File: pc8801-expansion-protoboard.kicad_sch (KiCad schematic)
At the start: 42 parts, among them J1 Solder Side, J2 Parts Side, J3 5V, J4 12V, J5 -12V, J6 GND_1, J7 GND_2, SW1 Reset ESP, U1 ExpansionEdge, U10 74LS165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

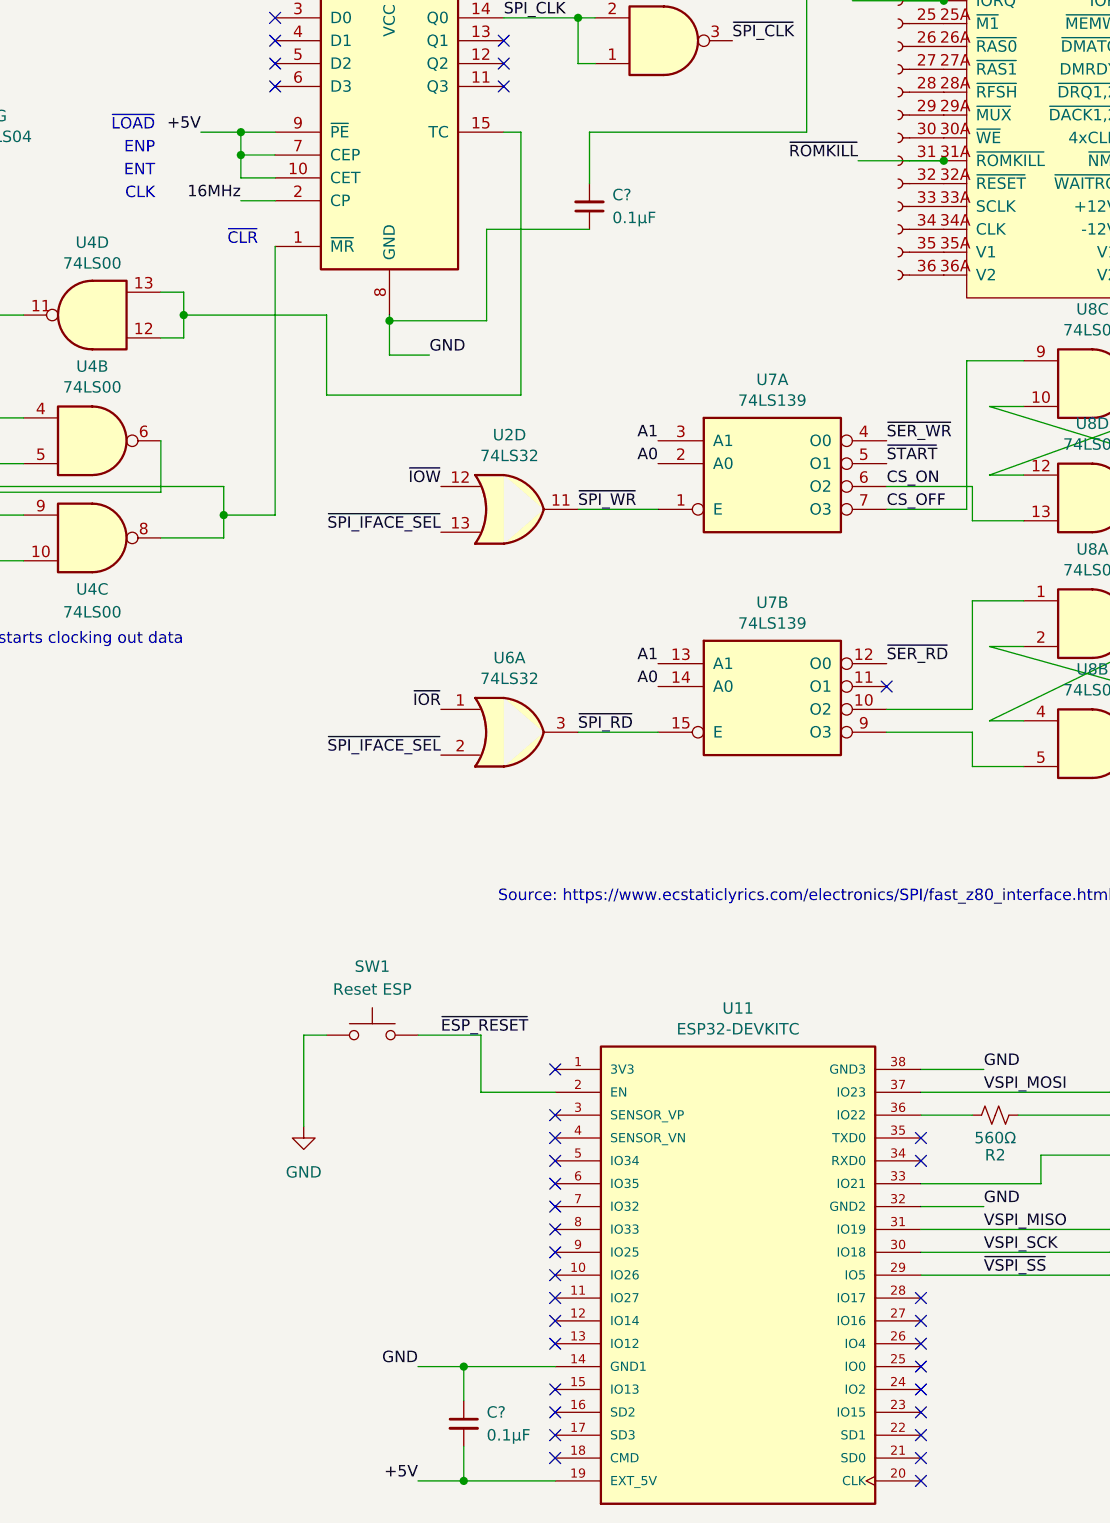
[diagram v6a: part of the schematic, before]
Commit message: Wire ESP32 to system reset
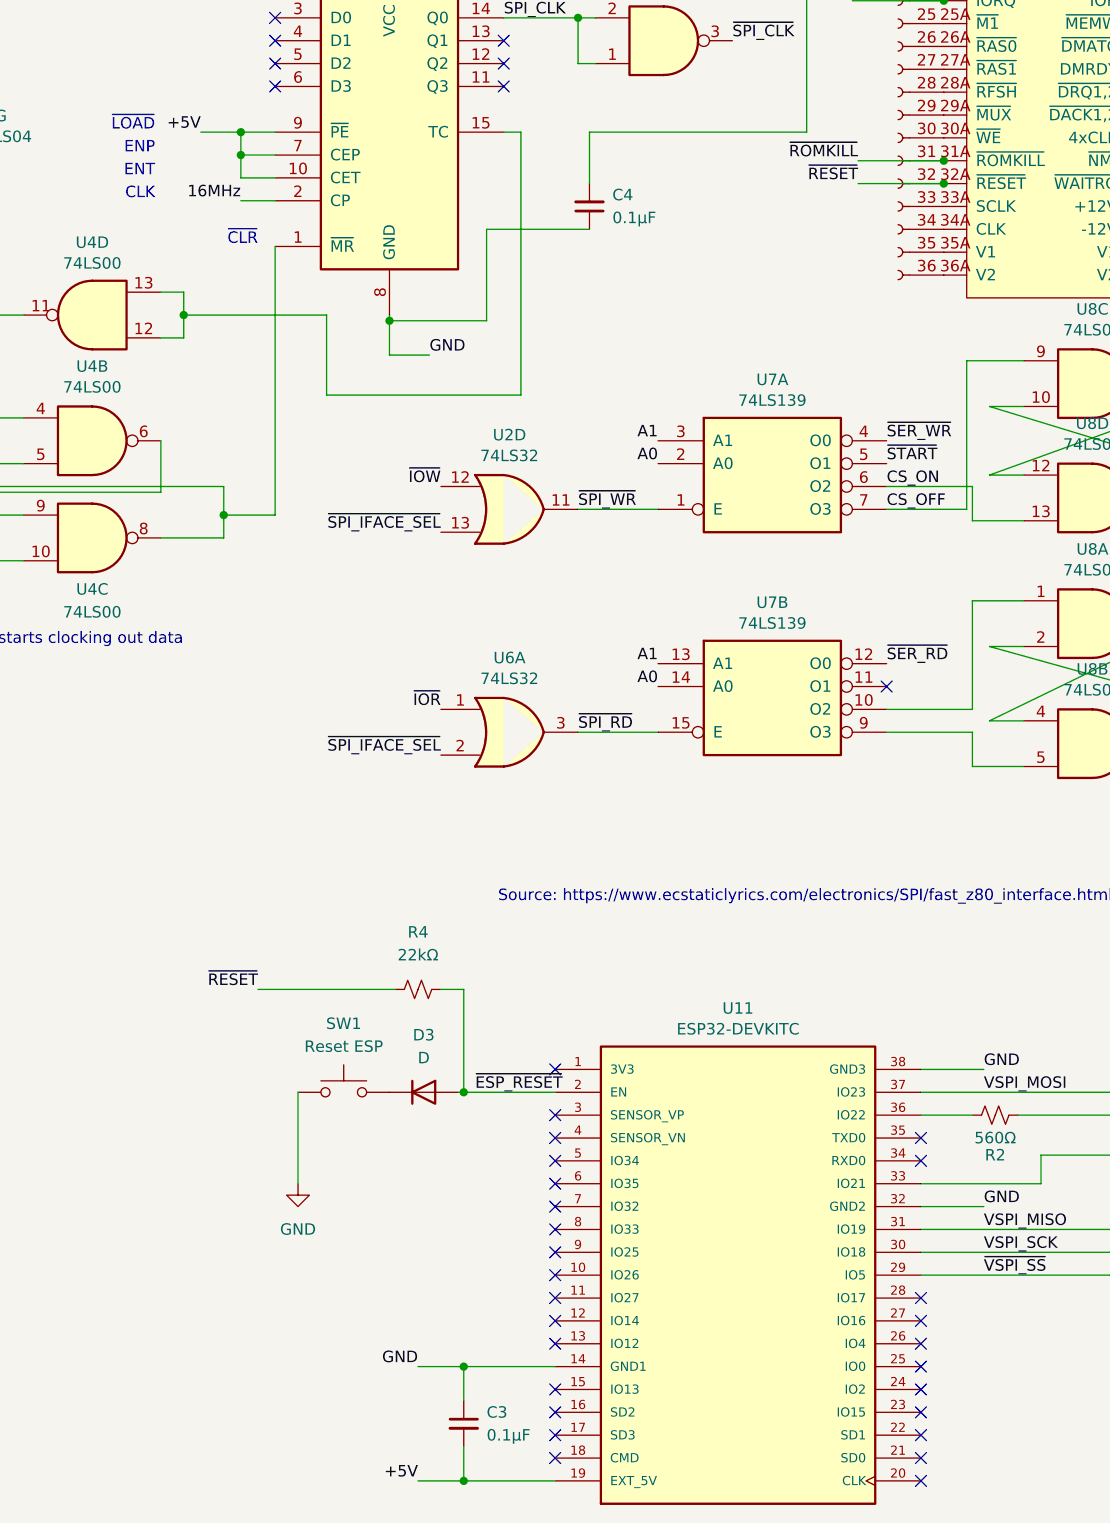
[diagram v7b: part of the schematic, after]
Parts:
- added D3: D, Diode_THT:D_A-405_P10.16mm_Horizontal, symbol Device:D
- added R4: 22kΩ, Resistor_THT:R_Axial_DIN0207_L6.3mm_D2.5mm_P10.16mm_Horizontal, symbol Device:R_Small_US
- gave numbers to parts that had none: 2
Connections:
- net ~{ESP_RESET}: now also D3.2 (A), R4.2; no longer SW1.2
- net ~{RESET}: now reaches J1.32 (Pin_32), U1.32A (~{RESET})
- net ~{RESET}: now also R4.1
- new net: D3.1 (K), SW1.2
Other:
- moved on the sheet: SW1
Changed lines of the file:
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@@
   (junction (at 135.89 60.325) (diameter 0) (color 0 0 0 0)
   )
+  (junction (at 82.55 227.33) (diameter 0) (color 0 0 0 0)
+  )
   (junction (at 135.89 123.825) (diameter 0) (color 0 0 0 0)
   )
@@
   )
   (junction (at 158.75 80.645) (diameter 0) (color 0 0 0 0)
+  )
+  (junction (at 135.89 126.365) (diameter 0) (color 0 0 0 0)
   )
   (junction (at 178.435 47.625) (diameter 0) (color 0 0 0 0)
@@
     (stroke (width 0) (type default) (color 0 0 0 0))
   )
-  (wire (pts (xy 84.455 227.33) (xy 84.455 220.98))
-    (stroke (width 0) (type default) (color 0 0 0 0))
-  )
   (wire (pts (xy 135.89 70.485) (xy 111.76 70.485))
     (stroke (width 0) (type default) (color 0 0 0 0))
@@
     (stroke (width 0) (type default) (color 0 0 0 0))
   )
+  (wire (pts (xy 80.01 215.9) (xy 82.55 215.9))
+    (stroke (width 0) (type default) (color 0 0 0 0))
+  )
   (wire (pts (xy 138.43 146.05) (xy 144.78 146.05))
     (stroke (width 0) (type default) (color 0 0 0 0))
@@
     (stroke (width 0) (type default) (color 0 0 0 0))
   )
+  (wire (pts (xy 82.55 215.9) (xy 82.55 227.33))
+    (stroke (width 0) (type default) (color 0 0 0 0))
+  )
   (wire (pts (xy 231.14 133.35) (xy 253.365 133.35))
     (stroke (width 0) (type default) (color 0 0 0 0))
@@
     (stroke (width 0) (type default) (color 0 0 0 0))
   )
-  (wire (pts (xy 64.77 220.98) (xy 67.31 220.98))
+  (wire (pts (xy 59.69 215.9) (xy 74.93 215.9))
     (stroke (width 0) (type default) (color 0 0 0 0))
   )
@@
     (stroke (width 0) (type default) (color 0 0 0 0))
   )
+  (wire (pts (xy 82.55 227.33) (xy 92.71 227.33))
+    (stroke (width 0) (type default) (color 0 0 0 0))
+  )
   (wire (pts (xy 303.53 114.3) (xy 305.435 114.3))
     (stroke (width 0) (type default) (color 0 0 0 0))
@@
     (stroke (width 0) (type default) (color 0 0 0 0))
   )
-  (wire (pts (xy 64.77 231.14) (xy 64.77 220.98))
+  (wire (pts (xy 64.135 237.49) (xy 64.135 227.33))
     (stroke (width 0) (type default) (color 0 0 0 0))
   )
@@
     (stroke (width 0) (type default) (color 0 0 0 0))
   )
-  (wire (pts (xy 92.71 227.33) (xy 84.455 227.33))
+  (wire (pts (xy 81.915 227.33) (xy 82.55 227.33))
     (stroke (width 0) (type default) (color 0 0 0 0))
   )
@@
     (stroke (width 0) (type default) (color 0 0 0 0))
   )
+  (wire (pts (xy 126.365 126.365) (xy 135.89 126.365))
+    (stroke (width 0) (type default) (color 0 0 0 0))
+  )
   (wire (pts (xy 209.55 133.35) (xy 187.325 133.35))
     (stroke (width 0) (type default) (color 0 0 0 0))
@@
   )
   (wire (pts (xy 158.75 85.725) (xy 188.595 85.725))
-    (stroke (width 0) (type default) (color 0 0 0 0))
-  )
-  (wire (pts (xy 84.455 220.98) (xy 77.47 220.98))
     (stroke (width 0) (type default) (color 0 0 0 0))
   )
@@
     (effects (font (size 1.27 1.27)) (justify right bottom))
   )
+  (label "~{RESET}" (at 126.365 126.365 180)
+    (effects (font (size 1.27 1.27)) (justify right bottom))
+  )
   (label "~{IORQ}" (at 125.73 106.045 180)
     (effects (font (size 1.27 1.27)) (justify right bottom))
@@
     (effects (font (size 1.27 1.27)) (justify left bottom))
   )
+  (label "~{RESET}" (at 59.69 215.9 180)
+    (effects (font (size 1.27 1.27)) (justify right bottom))
+  )
   (label "SPI_CLK" (at 86.995 107.95 0)
     (effects (font (size 1.27 1.27)) (justify left bottom))
@@
     (effects (font (size 1.27 1.27)) (justify left bottom))
   )
-  (label "~{ESP_RESET}" (at 80.01 220.98 0)
+  (label "~{ESP_RESET}" (at 83.82 227.33 0)
     (effects (font (size 1.27 1.27)) (justify left bottom))
   )
@@
   (symbol (lib_id "Device:C_Small") (at 82.55 264.16 0) (mirror y) (unit 1)
     (in_bom yes) (on_board yes) (fields_autoplaced)
-    (property "Reference" "C?" (id 0) (at 85.09 262.8962 0)
+    (property "Reference" "C3" (id 0) (at 85.09 262.8962 0)
       (effects (font (size 1.27 1.27)) (justify right))
     )
@@
     (pin "2")
   )
-  (symbol (lib_id "power:GND") (at 64.77 231.14 0) (unit 1)
+  (symbol (lib_id "power:GND") (at 64.135 237.49 0) (unit 1)
     (in_bom yes) (on_board yes) (fields_autoplaced)
-    (property "Reference" "#PWR0101" (id 0) (at 64.77 237.49 0)
-      (effects (font (size 1.27 1.27)) hide)
-    )
-    (property "Value" "GND" (id 1) (at 64.77 236.22 0))
-    (property "Footprint" "" (id 2) (at 64.77 231.14 0)
-      (effects (font (size 1.27 1.27)) hide)
-    )
-    (property "Datasheet" "" (id 3) (at 64.77 231.14 0)
+    (property "Reference" "#PWR0101" (id 0) (at 64.135 243.84 0)
+      (effects (font (size 1.27 1.27)) hide)
+    )
+    (property "Value" "GND" (id 1) (at 64.135 242.57 0))
+    (property "Footprint" "" (id 2) (at 64.135 237.49 0)
+      (effects (font (size 1.27 1.27)) hide)
+    )
+    (property "Datasheet" "" (id 3) (at 64.135 237.49 0)
       (effects (font (size 1.27 1.27)) hide)
     )
@@
   (symbol (lib_id "Device:C_Small") (at 96.52 128.905 180) (unit 1)
     (in_bom yes) (on_board yes) (fields_autoplaced)
-    (property "Reference" "C?" (id 0) (at 99.06 127.6285 0)
+    (property "Reference" "C4" (id 0) (at 99.06 127.6285 0)
       (effects (font (size 1.27 1.27)) (justify right))
     )
@@
     (pin "2")
   )
-  (symbol (lib_id "Switch:SW_Push") (at 72.39 220.98 0) (unit 1)
+  (symbol (lib_id "Switch:SW_Push") (at 69.215 227.33 0) (unit 1)
     (in_bom yes) (on_board yes) (fields_autoplaced)
-    (property "Reference" "SW1" (id 0) (at 72.39 213.36 0))
-    (property "Value" "Reset ESP" (id 1) (at 72.39 215.9 0))
-    (property "Footprint" "Button_Switch_THT:SW_PUSH_6mm" (id 2) (at 72.39 215.9 0)
-      (effects (font (size 1.27 1.27)) hide)
-    )
-    (property "Datasheet" "~" (id 3) (at 72.39 215.9 0)
+    (property "Reference" "SW1" (id 0) (at 69.215 219.71 0))
+    (property "Value" "Reset ESP" (id 1) (at 69.215 222.25 0))
+    (property "Footprint" "Button_Switch_THT:SW_PUSH_6mm" (id 2) (at 69.215 222.25 0)
+      (effects (font (size 1.27 1.27)) hide)
+    )
+    (property "Datasheet" "~" (id 3) (at 69.215 222.25 0)
       (effects (font (size 1.27 1.27)) hide)
     )
@@
     (pin "2")
   )
+  (symbol (lib_id "Device:R_Small_US") (at 77.47 215.9 90) (unit 1)
+    (in_bom yes) (on_board yes) (fields_autoplaced)
+    (property "Reference" "R4" (id 0) (at 77.47 209.55 90))
+    (property "Value" "22kΩ" (id 1) (at 77.47 212.09 90))
+    (property "Footprint" "Resistor_THT:R_Axial_DIN0207_L6.3mm_D2.5mm_P10.16mm_Horizontal" (id 2) (at 77.47 215.9 0)
+      (effects (font (size 1.27 1.27)) hide)
+    )
+    (property "Datasheet" "~" (id 3) (at 77.47 215.9 0)
+      (effects (font (size 1.27 1.27)) hide)
+    )
+    (pin "1")
+    (pin "2")
+  )
+  (symbol (lib_id "Device:D") (at 78.105 227.33 0) (unit 1)
+    (in_bom yes) (on_board yes) (fields_autoplaced)
+    (property "Reference" "D3" (id 0) (at 78.105 220.98 0))
+    (property "Value" "D" (id 1) (at 78.105 223.52 0))
+    (property "Footprint" "Diode_THT:D_A-405_P10.16mm_Horizontal" (id 2) (at 78.105 227.33 0)
+      (effects (font (size 1.27 1.27)) hide)
+    )
+    (property "Datasheet" "~" (id 3) (at 78.105 227.33 0)
+      (effects (font (size 1.27 1.27)) hide)
+    )
+    (pin "1")
+    (pin "2")
+  )
   (symbol (lib_id "Connector:TestPoint") (at 48.26 27.305 0) (unit 1)
     (in_bom yes) (on_board yes) (fields_autoplaced)
@@
     )
     (path "/52466011-5c1a-47bc-b32d-24022f04590a"
-      (reference "C?") (unit 1) (value "0.1µF") (footprint "Capacitor_THT:C_Disc_D5.0mm_W2.5mm_P2.50mm")
+      (reference "C3") (unit 1) (value "0.1µF") (footprint "Capacitor_THT:C_Disc_D5.0mm_W2.5mm_P2.50mm")
     )
     (path "/58a72614-8736-4d29-814c-480b5f42803b"
-      (reference "C?") (unit 1) (value "0.1µF") (footprint "Capacitor_THT:C_Disc_D5.0mm_W2.5mm_P2.50mm")
+      (reference "C4") (unit 1) (value "0.1µF") (footprint "Capacitor_THT:C_Disc_D5.0mm_W2.5mm_P2.50mm")
     )
     (path "/79af274b-03a2-4947-b1c3-eb23d037fb00"
@@
       (reference "D2") (unit 1) (value "LED") (footprint "LED_THT:LED_D3.0mm")
     )
+    (path "/df55ff5e-1001-4d8a-aea4-81f312e60c3c"
+      (reference "D3") (unit 1) (value "D") (footprint "Diode_THT:D_A-405_P10.16mm_Horizontal")
+    )
     (path "/00000000-0000-0000-0000-000061c06ab2"
       (reference "J1") (unit 1) (value "Solder Side") (footprint "Connector_PinHeader_2.54mm:PinHeader_1x36_P2.54mm_Vertical")
@@
       (reference "R3") (unit 1) (value "560Ω") (footprint "Resistor_THT:R_Axial_DIN0207_L6.3mm_D2.5mm_P10.16mm_Horizontal")
     )
+    (path "/97ef518e-f5a2-4d1d-8fc8-633c15f5ec28"
+      (reference "R4") (unit 1) (value "22kΩ") (footprint "Resistor_THT:R_Axial_DIN0207_L6.3mm_D2.5mm_P10.16mm_Horizontal")
+    )
     (path "/70f9fc47-c421-429e-8cdb-52e212c53c51"

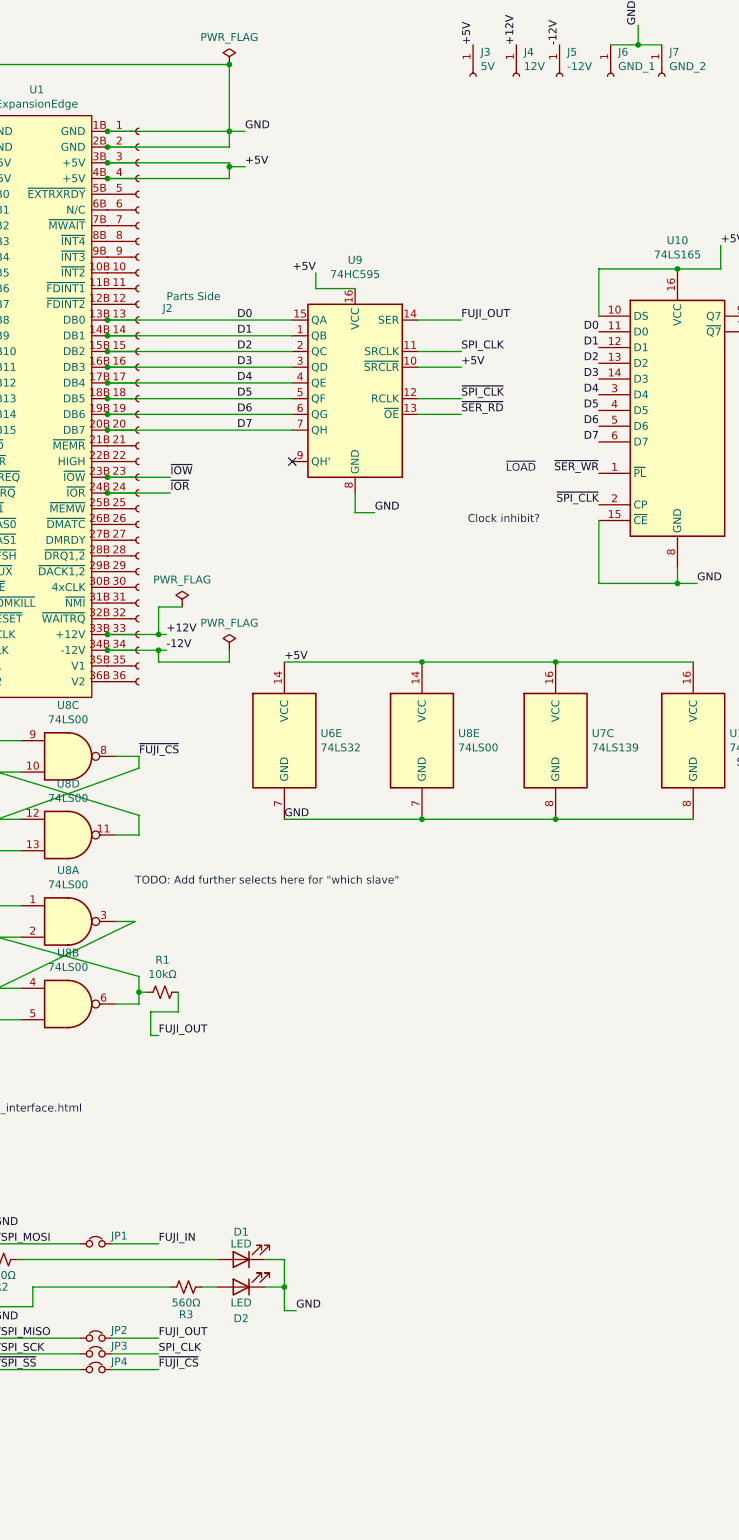
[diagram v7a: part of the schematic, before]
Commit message: As per Collapse, jumper-able clocks
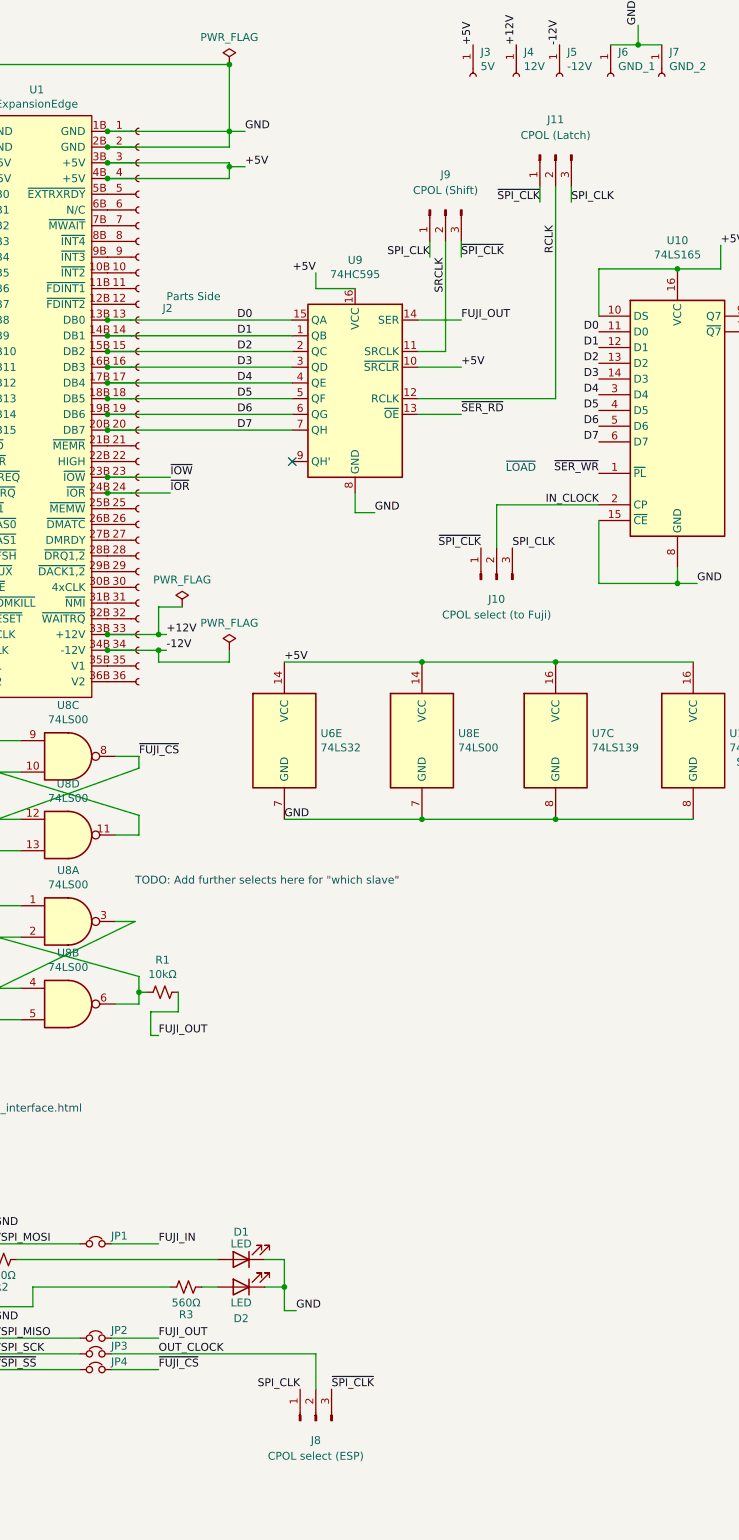
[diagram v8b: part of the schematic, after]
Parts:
- added J10: CPOL select (to Fuji), Connector_PinHeader_2.54mm:PinHeader_1x03_P2.54mm_Vertical, symbol Connector:Conn_01x03_Male
- added J11: CPOL (Latch), Connector_PinHeader_2.54mm:PinHeader_1x03_P2.54mm_Vertical, symbol Connector:Conn_01x03_Male
- added J8: CPOL select (ESP), Connector_PinHeader_2.54mm:PinHeader_1x03_P2.54mm_Vertical, symbol Connector:Conn_01x03_Male
- added J9: CPOL (Shift), Connector_PinHeader_2.54mm:PinHeader_1x03_P2.54mm_Vertical, symbol Connector:Conn_01x03_Male
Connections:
- net SPI_CLK: now also J10.3 (Pin_3), J11.3 (Pin_3), J8.1 (Pin_1), J9.1 (Pin_1); no longer JP3.2, U9.11 (SRCLK)
- net ~{SPI_CLK}: now also J10.1 (Pin_1), J11.1 (Pin_1), J8.3 (Pin_3), J9.3 (Pin_3); no longer U10.2 (CP), U9.12 (RCLK)
- new net IN_CLOCK: J10.2 (Pin_2), U10.2 (CP)
- new net OUT_CLOCK: J8.2 (Pin_2), JP3.2
- new net RCLK: J11.2 (Pin_2), U9.12 (RCLK)
- new net SRCLK: J9.2 (Pin_2), U9.11 (SRCLK)
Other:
- note removed: "Clock inhibit?"
